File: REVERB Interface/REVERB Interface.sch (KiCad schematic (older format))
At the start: 3 parts

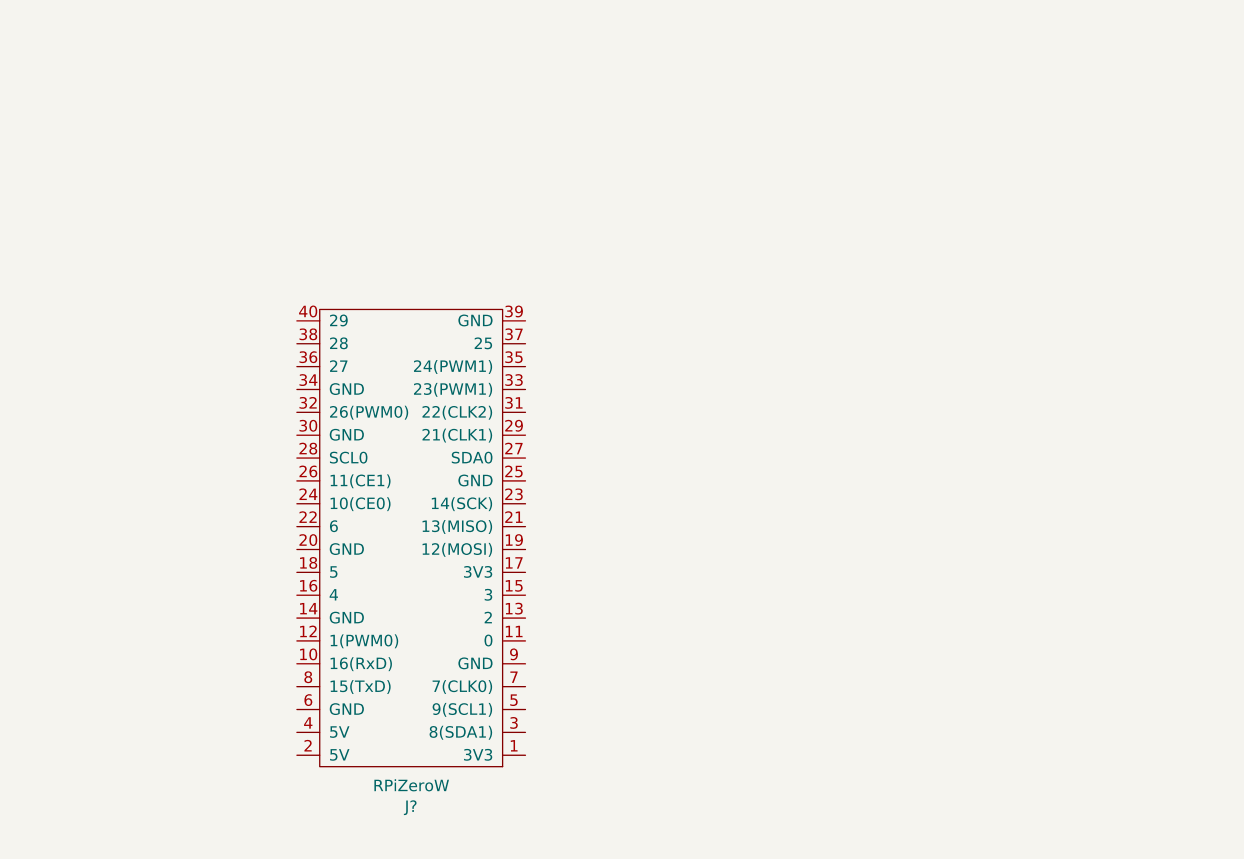
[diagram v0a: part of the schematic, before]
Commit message: mounting holes and ground connections
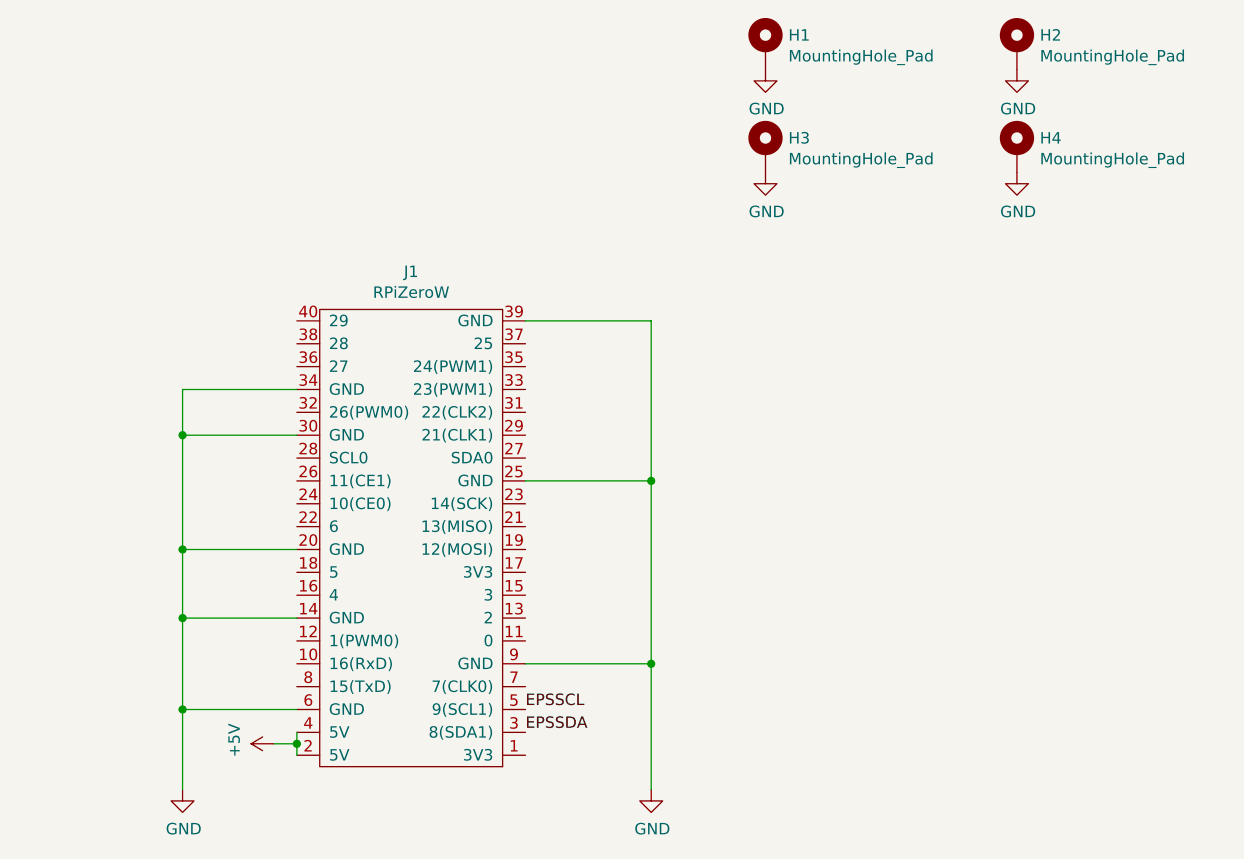
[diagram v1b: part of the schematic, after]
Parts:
- added H1, H2, H3, H4: MountingHole_Pad, symbol Mechanical:MountingHole_Pad
- gave numbers to parts that had none: 1
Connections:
- net +5V: now also J1.2 (5V), J1.4 (5V)
- net EPSSCL: now also J1.5 (9(SCL1))
- net EPSSDA: now also J1.3 (8(SDA1))
- net GND: now also J1.14 (GND), J1.20 (GND), J1.25 (GND), J1.30 (GND), J1.34 (GND), J1.39 (GND), J1.6 (GND), J1.9 (GND), H1.1, H2.1, H3.1, H4.1
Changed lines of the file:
@@
 $EndDescr
 $Comp
-L REVERBSym:RPiZeroW J?
+L REVERBSym:RPiZeroW J1
 U 1 1 615AB4AD
 P 6900 3900
-F 0 "J?" H 6900 4075 50  0000 C CNN
-F 1 "RPiZeroW" H 6900 3984 50  0000 C CNN
+F 0 "J1" H 6900 1735 50  0000 C CNN
+F 1 "RPiZeroW" H 6900 1826 50  0000 C CNN
 F 2 "" H 6900 3850 50  0001 C CNN
 F 3 "" H 6900 3850 50  0001 C CNN
@@
 Wire Notes Line
 	4300 750  850  750
+Text Label 7400 3650 0    50   ~ 0
+EPSSCL
+Text Label 7400 3750 0    50   ~ 0
+EPSSDA
+Wire Wire Line
+	6400 3750 6400 3800
+$Comp
+L power:+5V #PWR?
+U 1 1 615F78E4
+P 6300 3800
+F 0 "#PWR?" H 6300 3650 50  0001 C CNN
+F 1 "+5V" H 6315 3973 50  0000 C CNN
+F 2 "" H 6300 3800 50  0001 C CNN
+F 3 "" H 6300 3800 50  0001 C CNN
+	1    6300 3800
+	0    -1   -1   0
+$EndComp
+Wire Wire Line
+	6300 3800 6400 3800
+Connection ~ 6400 3800
+Wire Wire Line
+	6400 3800 6400 3850
+$Comp
+L Mechanical:MountingHole_Pad H1
+U 1 1 615FC76F
+P 8450 750
+F 0 "H1" H 8550 799 50  0000 L CNN
+F 1 "MountingHole_Pad" H 8550 708 50  0000 L CNN
+F 2 "" H 8450 750 50  0001 C CNN
+F 3 "~" H 8450 750 50  0001 C CNN
+	1    8450 750
+	1    0    0    -1
+$EndComp
+$Comp
+L Mechanical:MountingHole_Pad H3
+U 1 1 615FD785
+P 8450 1200
+F 0 "H3" H 8550 1249 50  0000 L CNN
+F 1 "MountingHole_Pad" H 8550 1158 50  0000 L CNN
+F 2 "" H 8450 1200 50  0001 C CNN
+F 3 "~" H 8450 1200 50  0001 C CNN
+	1    8450 1200
+	1    0    0    -1
+$EndComp
+$Comp
+L Mechanical:MountingHole_Pad H2
+U 1 1 615FDFBF
+P 9550 750
+F 0 "H2" H 9650 799 50  0000 L CNN
+F 1 "MountingHole_Pad" H 9650 708 50  0000 L CNN
+F 2 "" H 9550 750 50  0001 C CNN
+F 3 "~" H 9550 750 50  0001 C CNN
+	1    9550 750
+	1    0    0    -1
+$EndComp
+$Comp
+L Mechanical:MountingHole_Pad H4
+U 1 1 615FEAC9
+P 9550 1200
+F 0 "H4" H 9650 1249 50  0000 L CNN
+F 1 "MountingHole_Pad" H 9650 1158 50  0000 L CNN
+F 2 "" H 9550 1200 50  0001 C CNN
+F 3 "~" H 9550 1200 50  0001 C CNN
+	1    9550 1200
+	1    0    0    -1
+$EndComp
+$Comp
+L power:GND #PWR?
+U 1 1 6160138A
+P 9550 1300
+F 0 "#PWR?" H 9550 1050 50  0001 C CNN
+F 1 "GND" H 9555 1127 50  0000 C CNN
+F 2 "" H 9550 1300 50  0001 C CNN
+F 3 "" H 9550 1300 50  0001 C CNN
+	1    9550 1300
+	1    0    0    -1
+$EndComp
+$Comp
+L power:GND #PWR?
+U 1 1 61602AD3
+P 8450 1300
+F 0 "#PWR?" H 8450 1050 50  0001 C CNN
+F 1 "GND" H 8455 1127 50  0000 C CNN
+F 2 "" H 8450 1300 50  0001 C CNN
+F 3 "" H 8450 1300 50  0001 C CNN
+	1    8450 1300
+	1    0    0    -1
+$EndComp
+$Comp
+L power:GND #PWR?
+U 1 1 61602F50
+P 8450 850
+F 0 "#PWR?" H 8450 600 50  0001 C CNN
+F 1 "GND" H 8455 677 50  0000 C CNN
+F 2 "" H 8450 850 50  0001 C CNN
+F 3 "" H 8450 850 50  0001 C CNN
+	1    8450 850
+	1    0    0    -1
+$EndComp
+$Comp
+L power:GND #PWR?
+U 1 1 6160353D
+P 9550 850
+F 0 "#PWR?" H 9550 600 50  0001 C CNN
+F 1 "GND" H 9555 677 50  0000 C CNN
+F 2 "" H 9550 850 50  0001 C CNN
+F 3 "" H 9550 850 50  0001 C CNN
+	1    9550 850
+	1    0    0    -1
+$EndComp
+Wire Wire Line
+	6400 3650 5900 3650
+Wire Wire Line
+	5900 3650 5900 4000
+Wire Wire Line
+	6400 3250 5900 3250
+Wire Wire Line
+	5900 3250 5900 3650
+Connection ~ 5900 3650
+Wire Wire Line
+	6400 2950 5900 2950
+Wire Wire Line
+	5900 2950 5900 3250
+Connection ~ 5900 3250
+Wire Wire Line
+	6400 2450 5900 2450
+Wire Wire Line
+	5900 2450 5900 2950
+Connection ~ 5900 2950
+Wire Wire Line
+	6400 2250 5900 2250
+Wire Wire Line
+	5900 2250 5900 2450
+Connection ~ 5900 2450
+Wire Wire Line
+	7400 1950 7950 1950
+Wire Wire Line
+	7950 1950 7950 2650
+Wire Wire Line
+	7400 3450 7950 3450
+Connection ~ 7950 3450
+Wire Wire Line
+	7950 3450 7950 4000
+Wire Wire Line
+	7400 2650 7950 2650
+Connection ~ 7950 2650
+Wire Wire Line
+	7950 2650 7950 3450
+$Comp
+L power:GND #PWR?
+U 1 1 61608D37
+P 5900 4000
+F 0 "#PWR?" H 5900 3750 50  0001 C CNN
+F 1 "GND" H 5905 3827 50  0000 C CNN
+F 2 "" H 5900 4000 50  0001 C CNN
+F 3 "" H 5900 4000 50  0001 C CNN
+	1    5900 4000
+	1    0    0    -1
+$EndComp
+$Comp
+L power:GND #PWR?
+U 1 1 6160A077
+P 7950 4000
+F 0 "#PWR?" H 7950 3750 50  0001 C CNN
+F 1 "GND" H 7955 3827 50  0000 C CNN
+F 2 "" H 7950 4000 50  0001 C CNN
+F 3 "" H 7950 4000 50  0001 C CNN
+	1    7950 4000
+	1    0    0    -1
+$EndComp
 $EndSCHEMATC

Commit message: work
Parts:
- added J2: Iridium, symbol Connector_Generic:Conn_02x08_Odd_Even
- added J3: APRS, symbol Connector_Generic:Conn_02x10_Odd_Even
- added J4: Antenna, symbol Connector:Conn_01x09_Male
- added J5: USB, symbol Connector:Conn_01x02_Male
- added U1: AT25P, symbol Memory_EEPROM:AT25xxx
- added U2: MAX3232, symbol Interface_UART:MAX3232
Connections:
- new net D+: J5.1 (Pin_1)
- new net D-: J5.2 (Pin_2)
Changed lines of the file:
@@
+	1    0    0    -1
+$EndComp
+$Comp
+L Connector_Generic:Conn_02x08_Odd_Even J2
+U 1 1 615BBA54
+P 3850 5650
+F 0 "J2" H 3900 5025 50  0000 C CNN
+F 1 "Iridium" H 3900 5116 50  0000 C CNN
+F 2 "" H 3850 5650 50  0001 C CNN
+F 3 "~" H 3850 5650 50  0001 C CNN
+	1    3850 5650
+	-1   0    0    1
+$EndComp
+$Comp
+L Connector_Generic:Conn_02x10_Odd_Even J3
+U 1 1 615C1024
+P 2300 5450
+F 0 "J3" H 2350 6067 50  0000 C CNN
+F 1 "APRS" H 2350 5976 50  0000 C CNN
+F 2 "" H 2300 5450 50  0001 C CNN
+F 3 "~" H 2300 5450 50  0001 C CNN
+	1    2300 5450
+	1    0    0    -1
+$EndComp
+$Comp
+L Memory_EEPROM:AT25xxx U1
+U 1 1 615C353F
+P 6200 5650
+F 0 "U1" H 6200 6131 50  0000 C CNN
+F 1 "AT25P" H 6200 6040 50  0000 C CNN
+F 2 "" H 6200 5650 50  0001 C CNN
+F 3 "http://ww1.microchip.com/downloads/en/DeviceDoc/Atmel-8707-SEEPROM-AT25010B-020B-040B-Datasheet.pdf" H 6200 5650 50  0001 C CNN
+	1    6200 5650
+	1    0    0    -1
+$EndComp
+$Comp
+L Connector:Conn_01x09_Male J4
+U 1 1 615C48DD
+P 950 5400
+F 0 "J4" H 1058 5981 50  0000 C CNN
+F 1 "Antenna" H 1058 5890 50  0000 C CNN
+F 2 "" H 950 5400 50  0001 C CNN
+F 3 "~" H 950 5400 50  0001 C CNN
+	1    950  5400
+	1    0    0    -1
+$EndComp
+$Comp
+L Connector:Conn_01x02_Male J5
+U 1 1 615C5D8E
+P 9000 3100
+F 0 "J5" H 9108 3281 50  0000 C CNN
+F 1 "USB" H 9108 3190 50  0000 C CNN
+F 2 "" H 9000 3100 50  0001 C CNN
+F 3 "~" H 9000 3100 50  0001 C CNN
+	1    9000 3100
+	1    0    0    -1
+$EndComp
+Text Label 9200 3100 0    50   ~ 0
+D+
+Text Label 9200 3200 0    50   ~ 0
+D-
+$Comp
+L Interface_UART:MAX3232 U2
+U 1 1 615C8750
+P 8950 5950
+F 0 "U2" H 8950 7331 50  0000 C CNN
+F 1 "MAX3232" H 8950 7240 50  0000 C CNN
+F 2 "" H 9000 4900 50  0001 L CNN
+F 3 "https://datasheets.maximintegrated.com/en/ds/MAX3222-MAX3241.pdf" H 8950 6050 50  0001 C CNN
+	1    8950 5950
 	1    0    0    -1
 $EndComp

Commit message: work
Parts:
- added J5: MAX3232BOB, symbol Connector:Conn_01x10_Male
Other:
- moved on the sheet: U2
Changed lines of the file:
@@
 L Interface_UART:MAX3232 U2
 U 1 1 615C8750
-P 8950 5950
-F 0 "U2" H 8950 7331 50  0000 C CNN
-F 1 "MAX3232" H 8950 7240 50  0000 C CNN
-F 2 "" H 9000 4900 50  0001 L CNN
-F 3 "https://datasheets.maximintegrated.com/en/ds/MAX3222-MAX3241.pdf" H 8950 6050 50  0001 C CNN
-	1    8950 5950
+P 8800 5200
+F 0 "U2" H 8800 6581 50  0000 C CNN
+F 1 "MAX3232" H 8800 6490 50  0000 C CNN
+F 2 "" H 8850 4150 50  0001 L CNN
+F 3 "https://datasheets.maximintegrated.com/en/ds/MAX3222-MAX3241.pdf" H 8800 5300 50  0001 C CNN
+	1    8800 5200
 	1    0    0    -1
 $EndComp
+$Comp
+L Connector:Conn_01x10_Male J5
+U 1 1 615C6FC5
+P 10250 5700
+F 0 "J5" H 10358 6281 50  0000 C CNN
+F 1 "MAX3232BOB" H 10358 6190 50  0000 C CNN
+F 2 "" H 10250 5700 50  0001 C CNN
+F 3 "~" H 10250 5700 50  0001 C CNN
+	1    10250 5700
+	1    0    0    -1
+$EndComp

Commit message: work
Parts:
- added J6: USBSER2, symbol Connector:Conn_01x12_Male
- added J7: USBSER3, symbol Connector:Conn_01x06_Male
- added J8: USBSER1, symbol Connector:Conn_01x12_Male
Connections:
- net GND: now also J5.6 (Pin_6), U2.15 (GND)
- net R1OUT: now reaches J1.10 (16(RxD))
- net R1OUT: now also J5.9 (Pin_9), U2.12 (R1OUT)
- net T1IN: now reaches J1.8 (15(TxD))
- net T1IN: now also J5.7 (Pin_7), U2.11 (T1IN)
- net T1OUT: now reaches J5.1 (Pin_1)
- net T1OUT: now also U2.14 (T1OUT)
- net R1IN: now reaches J5.3 (Pin_3)
- net R1IN: now also U2.13 (R1IN)
- net MAX32PWR: now reaches J5.5 (Pin_5)
- net MAX32PWR: now also U2.16 (VCC)
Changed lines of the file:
@@
 	1    0    0    -1
 $EndComp
+$Comp
+L power:GND #PWR?
+U 1 1 615CEC17
+P 10450 5800
+F 0 "#PWR?" H 10450 5550 50  0001 C CNN
+F 1 "GND" H 10455 5627 50  0000 C CNN
+F 2 "" H 10450 5800 50  0001 C CNN
+F 3 "" H 10450 5800 50  0001 C CNN
+	1    10450 5800
+	0    -1   -1   0
+$EndComp
+Text Label 10450 5700 0    50   ~ 0
+MAX32PWR
+$Comp
+L power:GND #PWR?
+U 1 1 615D0A22
+P 8800 6400
+F 0 "#PWR?" H 8800 6150 50  0001 C CNN
+F 1 "GND" H 8805 6227 50  0000 C CNN
+F 2 "" H 8800 6400 50  0001 C CNN
+F 3 "" H 8800 6400 50  0001 C CNN
+	1    8800 6400
+	1    0    0    -1
+$EndComp
+Text Label 8800 4000 2    50   ~ 0
+MAX32PWR
+Text Label 10450 5900 0    50   ~ 0
+T1IN
+Text Label 10450 6100 0    50   ~ 0
+R1OUT
+Text Label 10450 5500 0    50   ~ 0
+R1IN
+Text Label 10450 5300 0    50   ~ 0
+T1OUT
+Text Label 9600 5300 0    50   ~ 0
+T1OUT
+Text Label 9600 5700 0    50   ~ 0
+R1IN
+Text Label 8000 5300 2    50   ~ 0
+T1IN
+Text Label 8000 5700 2    50   ~ 0
+R1OUT
+Text Label 6400 3450 2    50   ~ 0
+R1OUT
+Text Label 6400 3550 2    50   ~ 0
+T1IN
+$Comp
+L Connector:Conn_01x12_Male J6
+U 1 1 615D71F3
+P 4900 5550
+F 0 "J6" H 5008 6231 50  0000 C CNN
+F 1 "USBSER2" H 5008 6140 50  0000 C CNN
+F 2 "" H 4900 5550 50  0001 C CNN
+F 3 "~" H 4900 5550 50  0001 C CNN
+	1    4900 5550
+	1    0    0    -1
+$EndComp
+$Comp
+L Connector:Conn_01x12_Male J8
+U 1 1 615DA7A1
+P 4550 5650
+F 0 "J8" H 4750 4850 50  0000 R CNN
+F 1 "USBSER1" H 4850 4950 50  0000 R CNN
+F 2 "" H 4550 5650 50  0001 C CNN
+F 3 "~" H 4550 5650 50  0001 C CNN
+	1    4550 5650
+	-1   0    0    1
+$EndComp
+$Comp
+L Connector:Conn_01x06_Male J7
+U 1 1 615DBA1F
+P 4800 6400
+F 0 "J7" V 4862 6644 50  0000 L CNN
+F 1 "USBSER3" V 4953 6644 50  0000 L CNN
+F 2 "" H 4800 6400 50  0001 C CNN
+F 3 "~" H 4800 6400 50  0001 C CNN
+	1    4800 6400
+	0    1    1    0
+$EndComp
 $EndSCHEMATC
